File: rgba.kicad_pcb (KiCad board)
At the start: 4 copper layers, 40 x 23 mm, 76 parts, among them J1 CHARGE CONN, J10 UART_RTS, J11 Screw 1, J12 Screw 1, J2 BATT CONN, J3 UART_GND, J4 R SPK OUT, J5 L SPK OUT, J6 UART_CTS, J7 UART_VBUS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

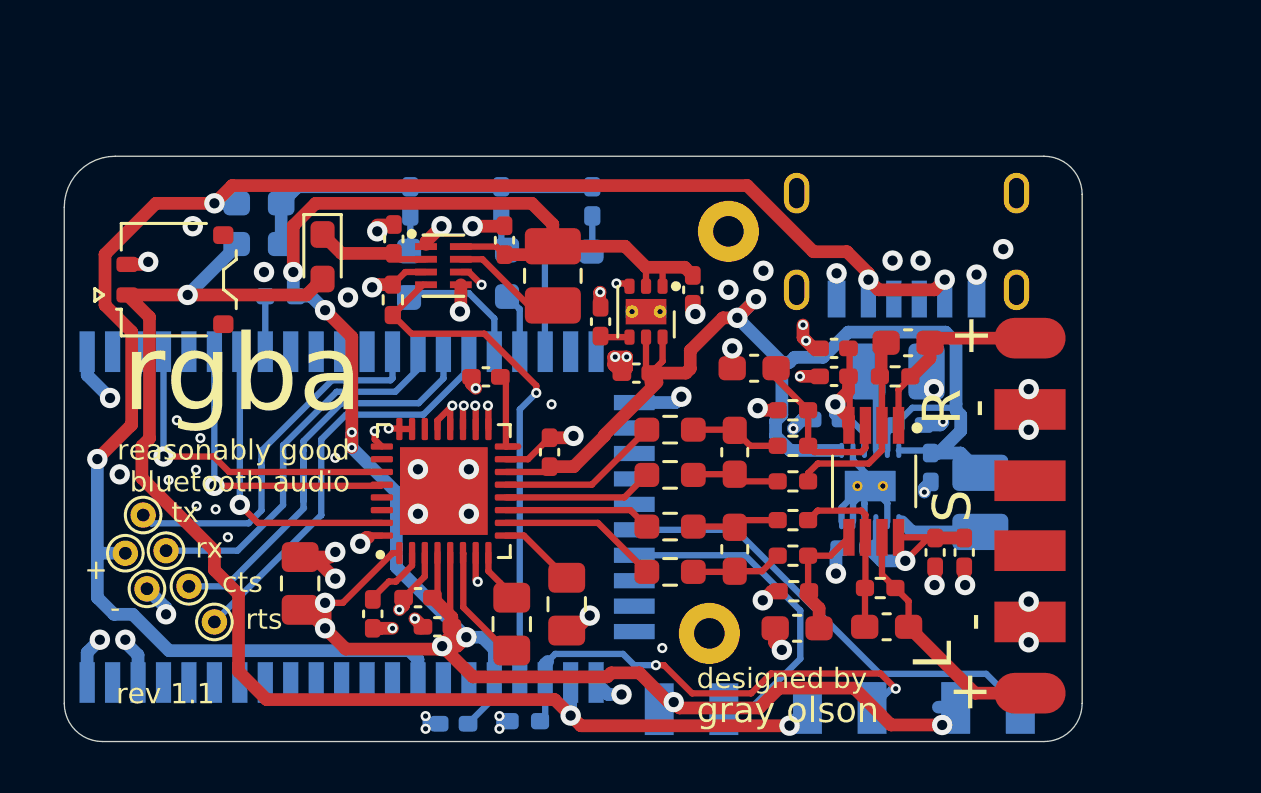
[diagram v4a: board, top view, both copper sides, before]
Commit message: modify uart header and led position
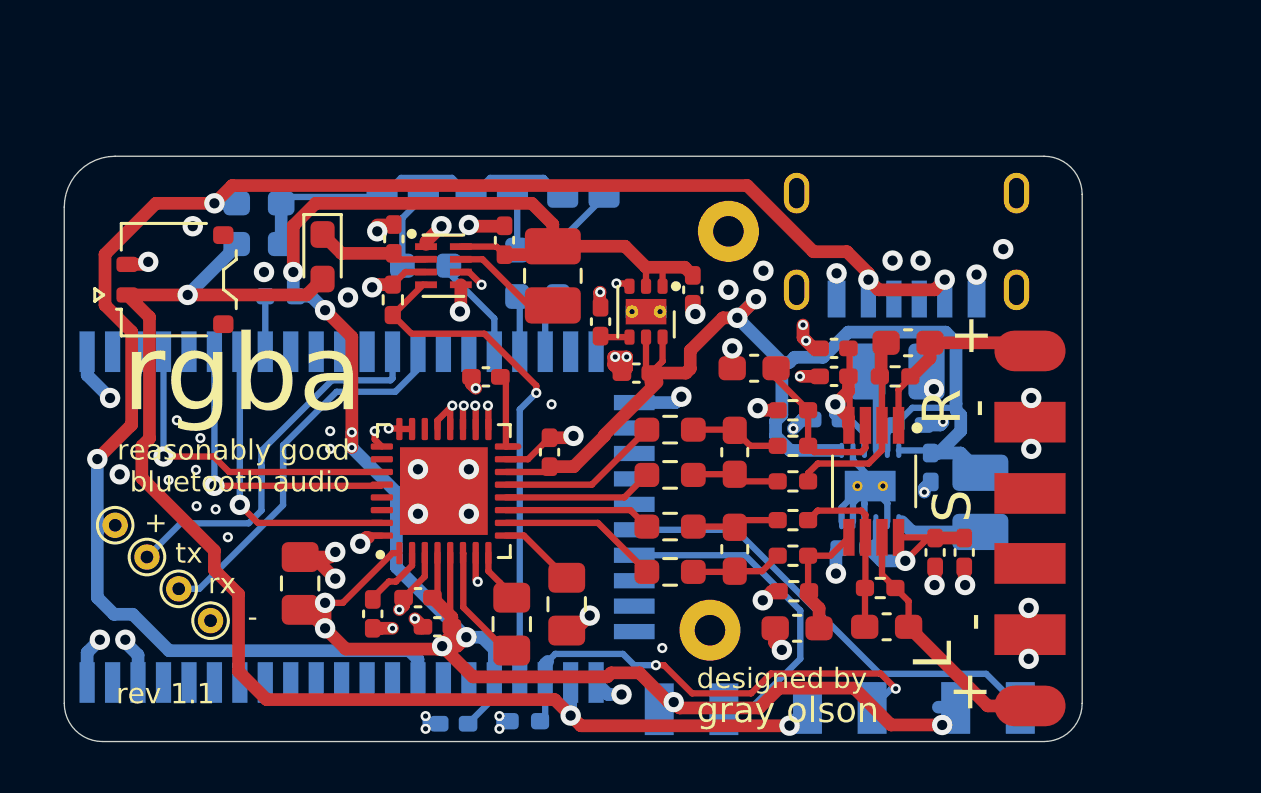
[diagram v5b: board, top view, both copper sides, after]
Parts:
- removed J10: UART_RTS, TestPoint:TestPoint_THTPad_D1.0mm_Drill0.5mm
- removed the J11 at (104.8, 111.2)
- removed J6: UART_CTS, TestPoint:TestPoint_THTPad_D1.0mm_Drill0.5mm
- added J12: Screw 1, rgba:MountingHole_1.2mm_M1_Pad, F.Cu at (104.9, 111.1)
- LED1, LED2, LED3: footprint LED_SMD:LED_0402_1005Metric_Pad0.77x0.64mm_HandSolder -> LED_SMD:LED_0603_1608Metric_Castellated
- U1: footprint Feasycom:FSC-BT806 -> rgba:FSC-BT806
- U5: footprint Package_SON:WSON-12-1EP_3x3mm_P0.45mm_EP1.2x2mm -> rgba:WSON-12-1EP_3x3mm_P0.45mm_EP1.2x2mm
- moved J3 2.80 mm to (85.2, 110.8)
- moved J8 1.66 mm to (82.8, 108.2)
- moved J9 1.58 mm to (84.0, 109.5)
- moved J7 1.17 mm to (81.5, 107.0)
- moved R3 0.94 mm to (98.9, 97.1), turned to 270 degrees
- moved R1 0.73 mm to (93.7, 96.8), turned to 0 degrees
- moved J4 0.50 mm to (117.5, 100.2)
- moved J5 0.50 mm to (117.5, 114.1)
- moved LED2 0.41 mm to (96.3, 94.1), turned to 180 degrees
- moved R2 0.40 mm to (97.3, 97.1)
- moved LED3 0.39 mm to (99.9, 94.1), turned to 180 degrees
- moved LED1 0.35 mm to (92.8, 94.1), turned to 180 degrees
- renumbered J12 to J11
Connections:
- U1 pad 15: UART_CTS -> Net-(U1-Pad15)
- U1 pad 16: UART_RTS -> Net-(U1-Pad16)
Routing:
- net UART_CTS: track 17.6 -> 0.00 mm
- net UART_RTS: track 16.5 -> 0.00 mm
- net LED_PWR: track 4.19 -> 2.37 mm
- net Net-(LED1-Pad1): track 1.53 -> 3.04 mm
- net Net-(LED3-Pad1): track 1.53 -> 2.84 mm
- net LED_CHG: track 5.21 -> 4.12 mm
- net GND: track 78.3 -> 77.3 mm
- net Net-(LED2-Pad1): track 1.53 -> 2.17 mm
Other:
- board text removed: "cts"
- board text removed: "rts"

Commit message: more size optimization
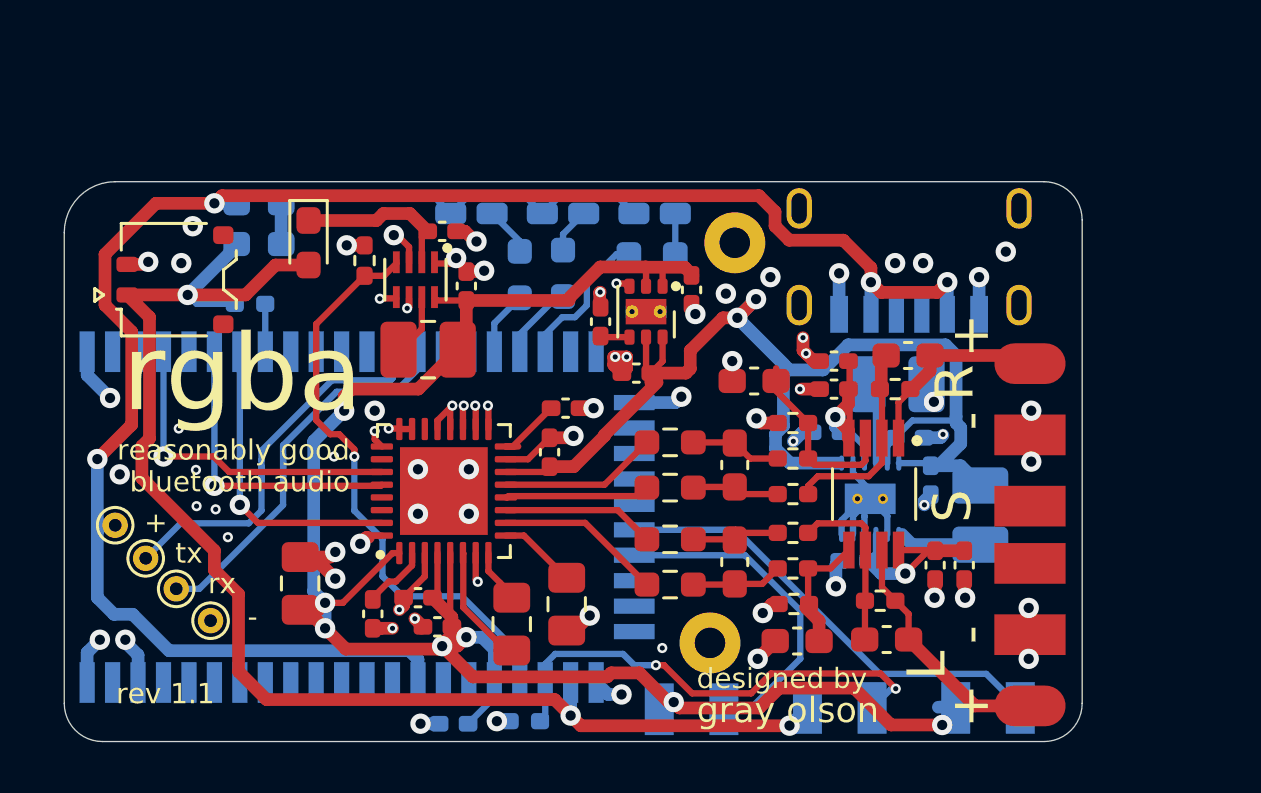
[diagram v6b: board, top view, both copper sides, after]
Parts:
- removed J9: UART_RX, TestPoint:TestPoint_THTPad_D1.0mm_Drill0.5mm
- added J6: UART_TX, TestPoint:TestPoint_THTPad_D1.0mm_Drill0.5mm, F.Cu at (82.7, 108.3)
- J8: value UART_TX -> UART_RX
- moved L30 5.69 mm to (93.8, 100.1), turned to 0 degrees
- moved R3 3.78 mm to (102.6, 96.3), turned to 180 degrees
- moved R1 3.72 mm to (97.4, 97.2), turned to 270 degrees
- moved C26 3.36 mm to (99.2, 102.4), turned to 180 degrees
- moved LED2 2.87 mm to (99.1, 94.8)
- moved LED3 2.87 mm to (102.7, 94.8)
- moved LED1 2.78 mm to (95.5, 94.8)
- moved C31 2.34 mm to (95.3, 97.6)
- moved C30 1.92 mm to (94.3, 95.5), turned to 0 degrees
- moved R30 1.90 mm to (91.3, 96.6)
- moved R2 1.80 mm to (99.1, 97.1)
- moved J8 1.70 mm to (83.9, 109.5)
- moved R10 1.24 mm to (86.8, 98.3), turned to 0 degrees
- moved U3 1.23 mm to (93.3, 97.3), turned to 270 degrees
- moved D30 0.78 mm to (89.1, 95.9)
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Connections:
- J8 pad 1: UART_TX -> UART_RX
- R10 pad 1: +3V3 -> VBAT
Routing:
- net +3V3: track 92.5 -> 77.8 mm, vias 10 -> 7
- net GND: track 77.3 -> 73.8 mm, vias 81 -> 76
- net LED_PWR: track 2.37 -> 5.77 mm
- net +3.3VA: track 45.4 -> 48.5 mm
- net +1V8: track 20.5 -> 23.2 mm
- net Net-(D1-Pad1): track 14.4 -> 17.1 mm
- net Net-(C30-Pad1): track 4.47 -> 6.45 mm
- net Net-(L30-Pad1): track 4.37 -> 2.49 mm
- net VBAT: track 52.5 -> 54.2 mm
- net LED_CHG: track 4.12 -> 2.67 mm
- net Net-(LED3-Pad1): track 2.84 -> 1.60 mm
- net Net-(LED1-Pad1): track 3.04 -> 1.94 mm
- net LED_CONN: track 2.21 -> 3.00 mm
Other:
- board size 40 x 23 mm -> 40 x 22 mm

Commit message: make UART terminals larger
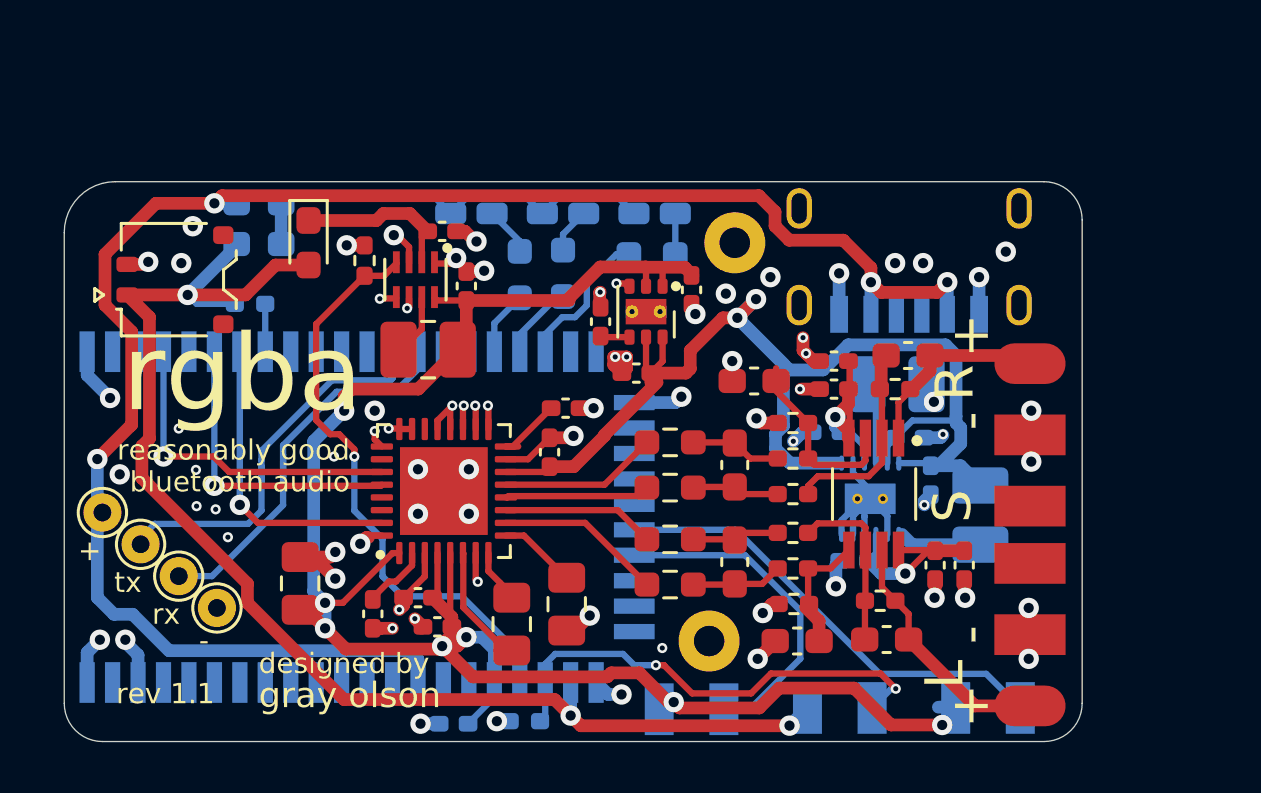
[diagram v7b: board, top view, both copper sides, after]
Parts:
- J3, J6, J7, J8: footprint TestPoint:TestPoint_THTPad_D1.0mm_Drill0.5mm -> rgba:TestPoint_THTPad_D1.5mm_Drill0.7mm
- moved J7 0.71 mm to (81.0, 106.5)
- moved J6 0.59 mm to (82.5, 107.8)
- moved J3 0.56 mm to (85.5, 110.2)
- moved J8 0.51 mm to (84.0, 109.0)
- moved J12 0.08 mm to (104.8, 111.5)
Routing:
- net VBAT: track 54.2 -> 52.4 mm
- net VBUS: track 68.5 -> 68.0 mm

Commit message: connect programming header power to 3v3 instead of vbus
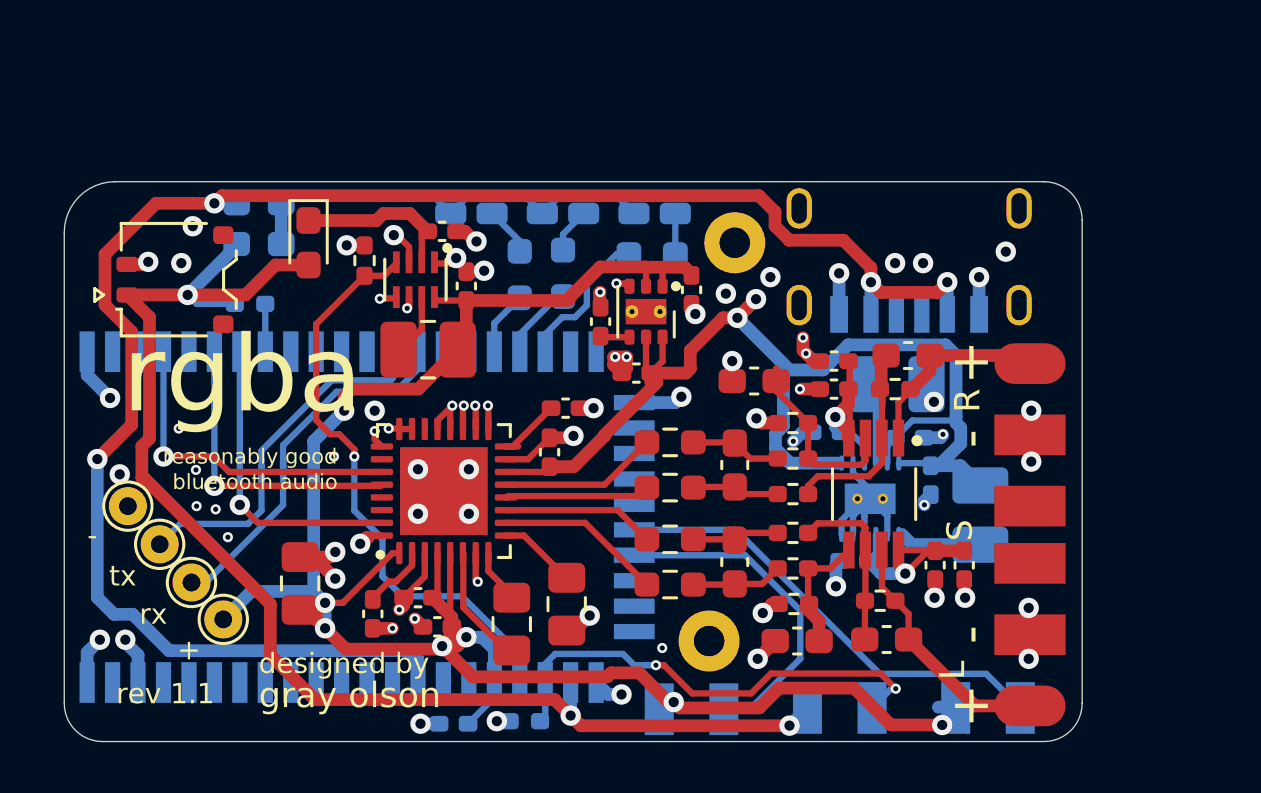
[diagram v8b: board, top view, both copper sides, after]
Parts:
- moved J7 6.34 mm to (85.8, 110.7)
- moved J3 5.32 mm to (82.0, 106.2)
- moved J6 0.75 mm to (83.2, 107.8)
- moved J8 0.56 mm to (84.5, 109.2)
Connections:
- J7 pad 1: VBUS -> +3V3
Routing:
- net +3V3: track 77.8 -> 81.8 mm
- net UART_TX: track 15.8 -> 14.8 mm
- net UART_RX: track 16.0 -> 15.1 mm
- net VBAT: track 52.4 -> 53.1 mm
